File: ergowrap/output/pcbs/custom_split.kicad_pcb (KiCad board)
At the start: 2 copper layers, 135.1 x 84 mm, 36 parts

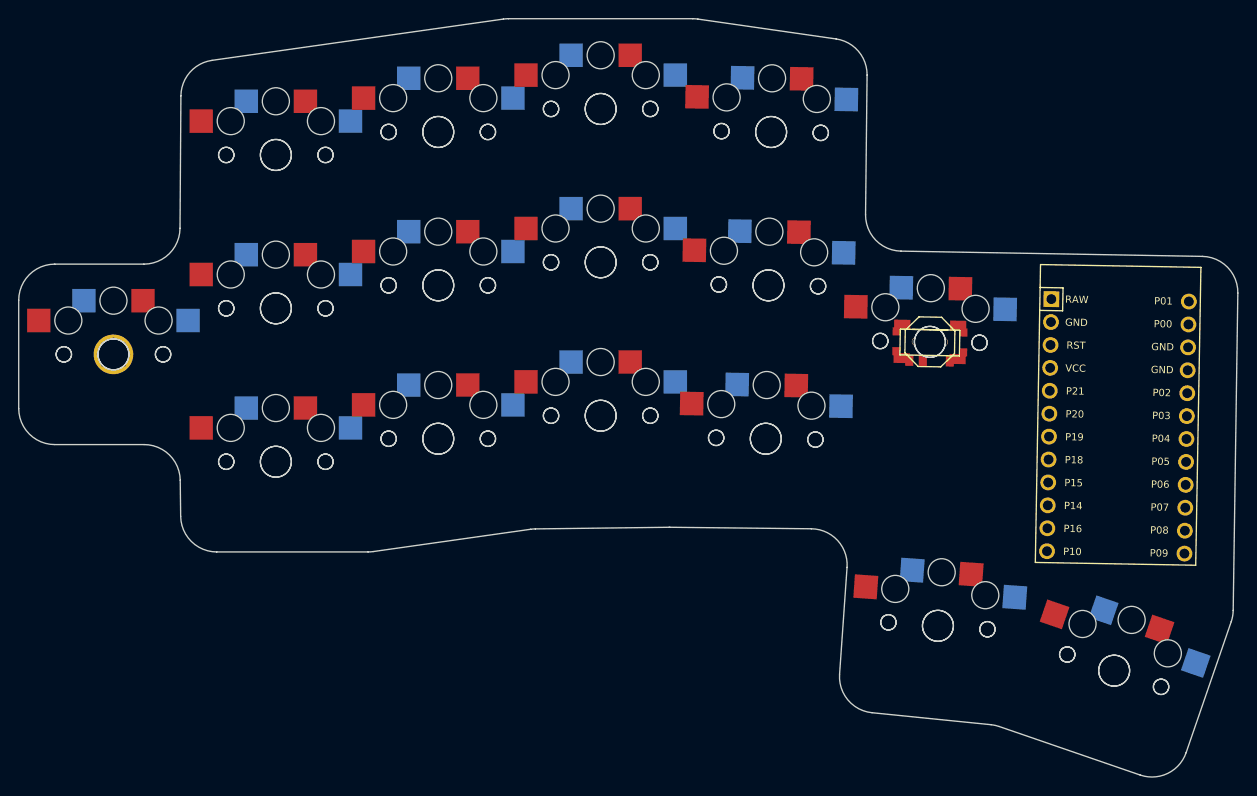
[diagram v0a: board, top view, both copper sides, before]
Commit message: Placed components, made case
Placed all of the necessary components on the board. Kept the 4 pad button instead of the 2 pad button. Added mounting holes. Created a case with standoffs to use on the bottom of the left half of the board. Need to go in and create a mirror.
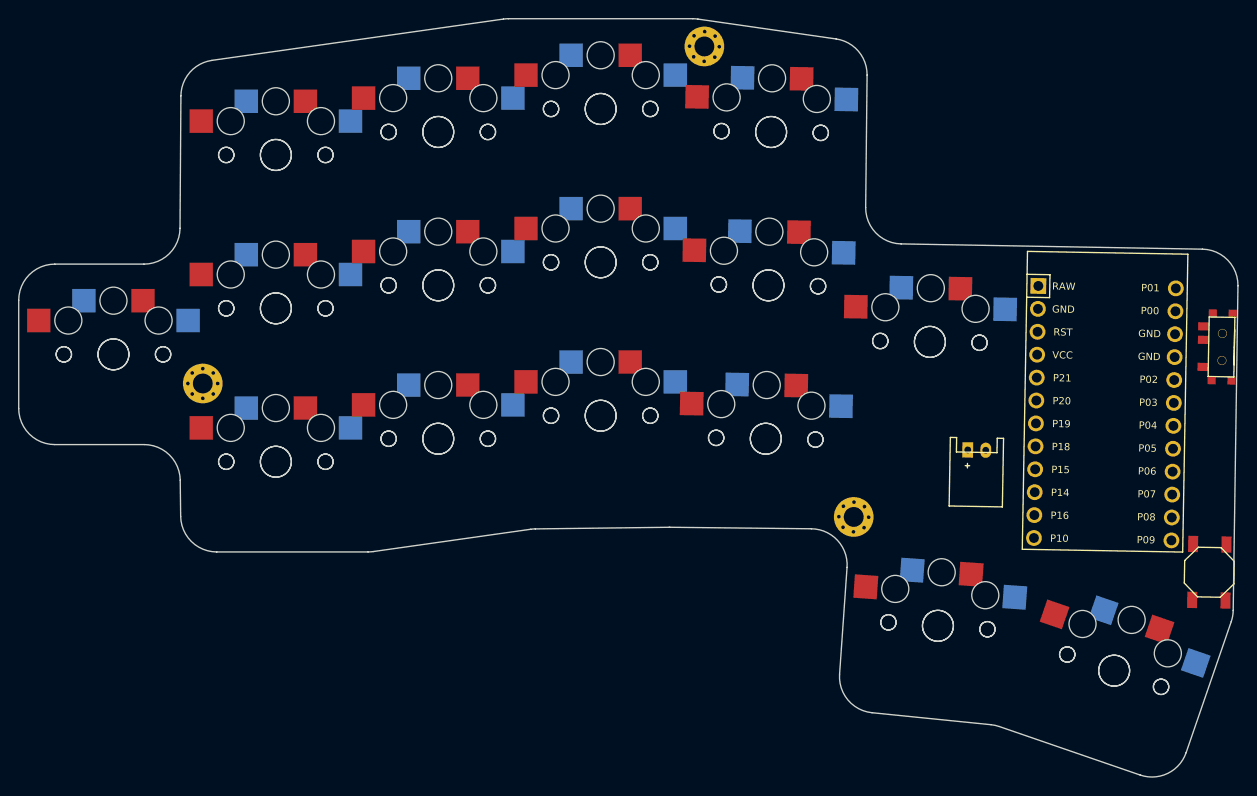
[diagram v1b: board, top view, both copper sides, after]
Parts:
- added JST1: , JST_PH_S2B-PH-K_02x2.00mm_Angled, F.Cu at (255.7, 163.6)
- added _2: , MountingHole_2.2mm_M2_Pad_Via, F.Cu at (225.5, 118.9)
- added _3: , MountingHole_2.2mm_M2_Pad_Via, F.Cu at (242.1, 171.0)
- moved B1 40.1 mm to (281.5, 177.2), turned to 89 degrees
- moved T1 32.4 mm to (282.9, 152.2), turned to -91 degrees
- moved _1 10.4 mm to (169.9, 156.2)
- moved MCU1 2.05 mm to (269.9, 159.5)
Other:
- outline, holes or cut-outs redrawn
